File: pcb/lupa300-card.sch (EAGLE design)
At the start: 22 parts

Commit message: more work on lupa card
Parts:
- added C13, C14, C15, C16, C17, C18, C19, C20, C21, C22, C25, C26, C27, C28, C29, C30, C5, C6: (no value), rcl:C-EUC0603
- added C23, C24: (no value), rcl:C-EUC1206
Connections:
- new net N$2: C25.2, C27.2
- net 2.5V: now also U$1.VADC1, U$1.VDDA, U$1.VDDD, U$1.VDDO
- net GND: now also C13.2, C14.2, C15.2, C16.2, C17.2, C18.2, C19.2, C20.2, C21.2, C22.2, C23.2, C24.2, C26.2, C28.2, C29.2, C30.2, C5.2, C6.2
- net VADC: now also C20.1, C21.1, C22.1; no longer U$1.VADC1
- net VDDA: now also C14.1, C15.1, C16.1; no longer U$1.VDDA
- net VDDD: now also C13.1, C5.1, C6.1; no longer U$1.VDDD
- net VDDO: now also C17.1, C18.1, C19.1; no longer U$1.VDDO
- net VPIX: now also C25.1, C26.1, C27.1
- net VRAW: now also C23.1, C24.1
- net VRESET_1: now also C28.1, C29.1, C30.1

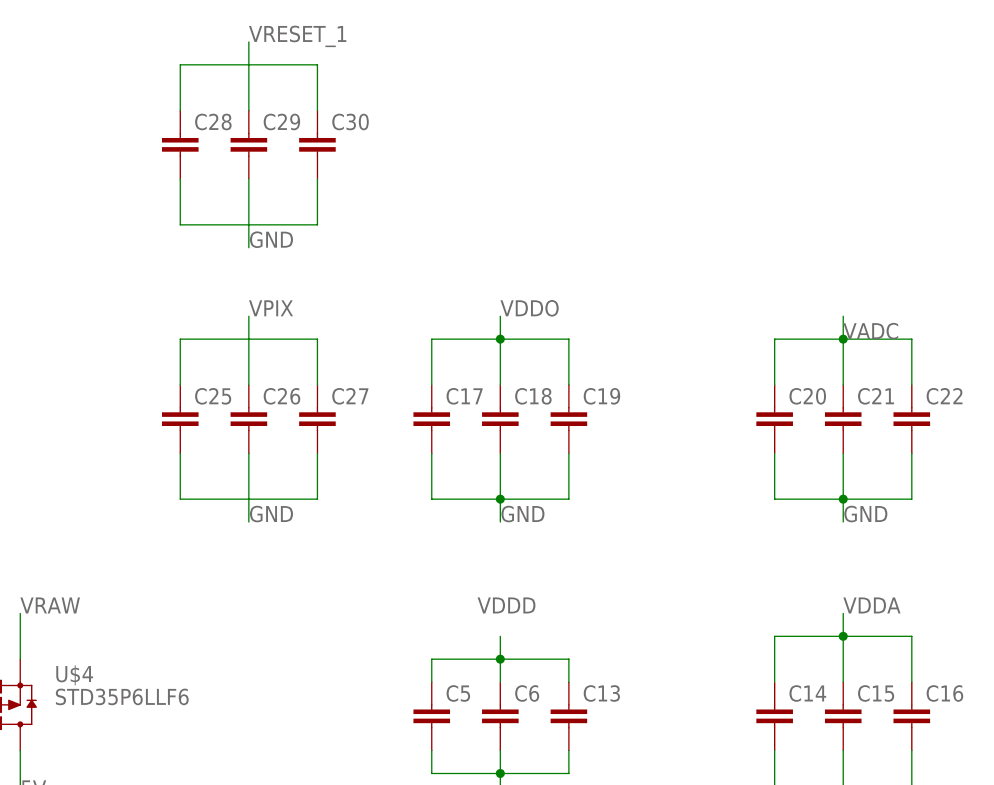
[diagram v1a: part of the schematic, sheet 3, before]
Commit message: made lupa card 4 layer
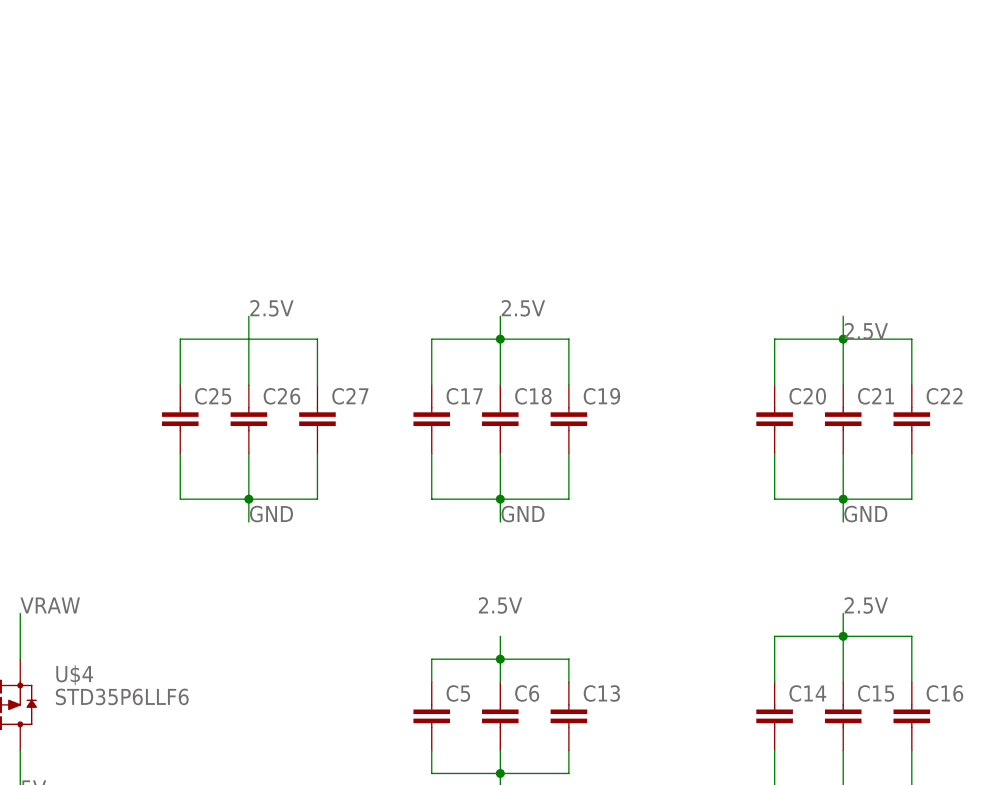
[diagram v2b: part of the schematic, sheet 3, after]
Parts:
- removed C28, C29, C30: (no value), rcl:C-EUC0603
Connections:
- removed net N$2: C25.2, C27.2
- removed net VADC: C20.1, C21.1, C22.1, R8.1, U$1.VADC, U$1.VADC2
- removed net VDDA: C14.1, C15.1, C16.1, R10.1, R11.1, R12.1, R9.1, U$1.VDDA1
- removed net VDDD: C13.1, C5.1, C6.1, U$1.VDDD1
- removed net VDDO: C17.1, C18.1, C19.1
- removed net VMEM_H: U$1.VMEM_H
- removed net VPIX: C25.1, C26.1, C27.1, R7.1, U$1.VPIX
- removed net VRESET_1: C28.1, C29.1, C30.1, U$1.VRESET_1
- net 2.5V: now also C13.1, C14.1, C15.1, C16.1, C17.1, C18.1, C19.1, C20.1, C21.1, C22.1, C25.1, C26.1, C27.1, C5.1, C6.1, R10.1, R11.1, R12.1, R7.1, R8.1, R9.1, U$1.VADC, U$1.VADC2, U$1.VDDA1, U$1.VDDD1, U$1.VPIX
- net 3V3: now also U$1.VMEM_H, U$1.VRESET_1
- net GND: now also C25.2, C27.2; no longer C28.2, C29.2, C30.2

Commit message: routed critical signals.
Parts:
- added C28, C29: (no value), rcl:C-EUC0603
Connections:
- net 3V3: now also C28.1, C29.1
- net GND: now also C28.2, C29.2
- net SPI_CLK: now also UZEDLOWER.14; no longer UZEDLOWER.3
- net SPI_DATA: now also UZEDLOWER.16; no longer UZEDLOWER.5
- net SPI_EN: now also UZEDLOWER.12; no longer UZEDLOWER.1
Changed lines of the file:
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@@
 <part name="C26" library="rcl" library_urn="urn:adsk.eagle:library:334" deviceset="C-EU" device="C0603" package3d_urn="urn:adsk.eagle:package:23616/2"/>
 <part name="C27" library="rcl" library_urn="urn:adsk.eagle:library:334" deviceset="C-EU" device="C0603" package3d_urn="urn:adsk.eagle:package:23616/2"/>
+<part name="C28" library="rcl" library_urn="urn:adsk.eagle:library:334" deviceset="C-EU" device="C0603" package3d_urn="urn:adsk.eagle:package:23616/2"/>
+<part name="C29" library="rcl" library_urn="urn:adsk.eagle:library:334" deviceset="C-EU" device="C0603" package3d_urn="urn:adsk.eagle:package:23616/2"/>
 </parts>
 <sheets>
@@
 <instance part="C26" gate="G$1" x="53.34" y="111.76"/>
 <instance part="C27" gate="G$1" x="60.96" y="111.76"/>
+<instance part="C28" gate="G$1" x="13.97" y="113.03"/>
+<instance part="C29" gate="G$1" x="22.86" y="113.03"/>
 </instances>
 <busses>
@@
 <junction x="53.34" y="101.6"/>
 </segment>
+<segment>
+<pinref part="C28" gate="G$1" pin="2"/>
+<wire x1="13.97" y1="107.95" x2="13.97" y2="104.14" width="0.1524" layer="91"/>
+<wire x1="13.97" y1="104.14" x2="17.78" y2="104.14" width="0.1524" layer="91"/>
+<pinref part="C29" gate="G$1" pin="2"/>
+<wire x1="17.78" y1="104.14" x2="22.86" y2="104.14" width="0.1524" layer="91"/>
+<wire x1="22.86" y1="104.14" x2="22.86" y2="107.95" width="0.1524" layer="91"/>
+<wire x1="17.78" y1="104.14" x2="17.78" y2="101.6" width="0.1524" layer="91"/>
+</segment>
 </net>
 <net name="3V3" class="0">
@@
 <wire x1="81.28" y1="40.64" x2="81.28" y2="45.72" width="0.1524" layer="91"/>
 <label x="81.28" y="45.72" size="1.778" layer="95"/>
+</segment>
+<segment>
+<pinref part="C29" gate="G$1" pin="1"/>
+<wire x1="22.86" y1="115.57" x2="22.86" y2="119.38" width="0.1524" layer="91"/>
+<wire x1="22.86" y1="119.38" x2="19.05" y2="119.38" width="0.1524" layer="91"/>
+<pinref part="C28" gate="G$1" pin="1"/>
+<wire x1="19.05" y1="119.38" x2="13.97" y2="119.38" width="0.1524" layer="91"/>
+<wire x1="13.97" y1="119.38" x2="13.97" y2="115.57" width="0.1524" layer="91"/>
+<wire x1="19.05" y1="119.38" x2="19.05" y2="121.92" width="0.1524" layer="91"/>
 </segment>
 </net>
@@
 </segment>
 </net>
-<net name="SPI_DATA" class="0">
-<segment>
-<pinref part="UZEDLOWER" gate="G$1" pin="5"/>
-<wire x1="55.88" y1="50.8" x2="50.8" y2="50.8" width="0.1524" layer="91"/>
-<label x="35.56" y="50.8" size="1.778" layer="95"/>
-</segment>
-</net>
-<net name="SPI_CLK" class="0">
-<segment>
-<pinref part="UZEDLOWER" gate="G$1" pin="3"/>
-<wire x1="55.88" y1="53.34" x2="50.8" y2="53.34" width="0.1524" layer="91"/>
-<label x="35.56" y="53.34" size="1.778" layer="95"/>
-</segment>
-</net>
-<net name="SPI_EN" class="0">
-<segment>
-<pinref part="UZEDLOWER" gate="G$1" pin="1"/>
-<wire x1="55.88" y1="55.88" x2="50.8" y2="55.88" width="0.1524" layer="91"/>
-<label x="35.56" y="55.88" size="1.778" layer="95"/>
-</segment>
-</net>
 <net name="VRAW" class="0">
 <segment>
@@
 </segment>
 </net>
+<net name="SPI_EN" class="0">
+<segment>
+<pinref part="UZEDLOWER" gate="G$1" pin="12"/>
+<wire x1="71.12" y1="43.18" x2="76.2" y2="43.18" width="0.1524" layer="91"/>
+<label x="78.74" y="43.18" size="1.778" layer="95"/>
+</segment>
+</net>
+<net name="SPI_CLK" class="0">
+<segment>
+<pinref part="UZEDLOWER" gate="G$1" pin="14"/>
+<wire x1="71.12" y1="40.64" x2="76.2" y2="40.64" width="0.1524" layer="91"/>
+<label x="78.74" y="40.64" size="1.778" layer="95"/>
+</segment>
+</net>
+<net name="SPI_DATA" class="0">
+<segment>
+<pinref part="UZEDLOWER" gate="G$1" pin="16"/>
+<wire x1="71.12" y1="38.1" x2="76.2" y2="38.1" width="0.1524" layer="91"/>
+<label x="78.74" y="38.1" size="1.778" layer="95"/>
+</segment>
+</net>

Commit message: finalized design
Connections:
- net FRAME_VALID: now also UZEDLOWER.12; no longer UZEDLOWER.10
- net INT_TIME1: now also UZEDLOWER.9; no longer UZEDLOWER.11
- net INT_TIME2: now also UZEDLOWER.10; no longer UZEDLOWER.13
- net INT_TIME3: now also UZEDLOWER.11; no longer UZEDLOWER.15
- net LINE_VALID: now also UZEDLOWER.13; no longer UZEDLOWER.9
- net SPI_CLK: now also UZEDLOWER.15; no longer UZEDLOWER.14
- net SPI_DATA: now also UZEDLOWER.14; no longer UZEDLOWER.16
- net SPI_EN: now also UZEDLOWER.16; no longer UZEDLOWER.12
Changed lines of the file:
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@@
 <?xml version="1.0" encoding="utf-8"?>
 <!DOCTYPE eagle SYSTEM "eagle.dtd">
-<eagle version="8.5.0">
+<eagle version="8.3.1">
 <drawing>
 <settings>
@@
 <wire x1="22.86" y1="104.14" x2="22.86" y2="107.95" width="0.1524" layer="91"/>
 <wire x1="17.78" y1="104.14" x2="17.78" y2="101.6" width="0.1524" layer="91"/>
+<label x="17.78" y="101.6" size="1.778" layer="95"/>
 </segment>
 </net>
@@
 <wire x1="13.97" y1="119.38" x2="13.97" y2="115.57" width="0.1524" layer="91"/>
 <wire x1="19.05" y1="119.38" x2="19.05" y2="121.92" width="0.1524" layer="91"/>
+<label x="19.05" y="121.92" size="1.778" layer="95"/>
 </segment>
 </net>
@@
 </segment>
 </net>
+<net name="VRAW" class="0">
+<segment>
+<pinref part="UZEDLOWER" gate="G$1" pin="7"/>
+<wire x1="55.88" y1="48.26" x2="50.8" y2="48.26" width="0.1524" layer="91"/>
+<label x="35.56" y="48.26" size="1.778" layer="95"/>
+</segment>
+<segment>
+<pinref part="UZEDLOWER" gate="G$1" pin="8"/>
+<wire x1="71.12" y1="48.26" x2="76.2" y2="48.26" width="0.1524" layer="91"/>
+<label x="78.74" y="48.26" size="1.778" layer="95"/>
+</segment>
+</net>
+<net name="MOSFET_CTRL" class="0">
+<segment>
+<pinref part="UZEDLOWER" gate="G$1" pin="6"/>
+<wire x1="86.36" y1="50.8" x2="71.12" y2="50.8" width="0.1524" layer="91"/>
+<label x="86.36" y="50.8" size="1.778" layer="95"/>
+</segment>
+</net>
 <net name="INT_TIME1" class="0">
+<segment>
+<pinref part="UZEDLOWER" gate="G$1" pin="9"/>
+<wire x1="55.88" y1="45.72" x2="50.8" y2="45.72" width="0.1524" layer="91"/>
+<label x="35.56" y="45.72" size="1.778" layer="95"/>
+</segment>
+</net>
+<net name="INT_TIME3" class="0">
 <segment>
 <pinref part="UZEDLOWER" gate="G$1" pin="11"/>
@@
 </segment>
 </net>
-<net name="INT_TIME2" class="0">
+<net name="LINE_VALID" class="0">
 <segment>
 <pinref part="UZEDLOWER" gate="G$1" pin="13"/>
@@
 </segment>
 </net>
-<net name="INT_TIME3" class="0">
+<net name="SPI_CLK" class="0">
 <segment>
 <pinref part="UZEDLOWER" gate="G$1" pin="15"/>
@@
 </segment>
 </net>
+<net name="SPI_EN" class="0">
+<segment>
+<pinref part="UZEDLOWER" gate="G$1" pin="16"/>
+<wire x1="71.12" y1="38.1" x2="76.2" y2="38.1" width="0.1524" layer="91"/>
+<label x="78.74" y="38.1" size="1.778" layer="95"/>
+</segment>
+</net>
+<net name="SPI_DATA" class="0">
+<segment>
+<pinref part="UZEDLOWER" gate="G$1" pin="14"/>
+<wire x1="71.12" y1="40.64" x2="76.2" y2="40.64" width="0.1524" layer="91"/>
+<label x="78.74" y="40.64" size="1.778" layer="95"/>
+</segment>
+</net>
 <net name="FRAME_VALID" class="0">
+<segment>
+<pinref part="UZEDLOWER" gate="G$1" pin="12"/>
+<wire x1="71.12" y1="43.18" x2="76.2" y2="43.18" width="0.1524" layer="91"/>
+<label x="78.74" y="43.18" size="1.778" layer="95"/>
+</segment>
+</net>
+<net name="INT_TIME2" class="0">
 <segment>
 <pinref part="UZEDLOWER" gate="G$1" pin="10"/>
 <wire x1="71.12" y1="45.72" x2="76.2" y2="45.72" width="0.1524" layer="91"/>
 <label x="78.74" y="45.72" size="1.778" layer="95"/>
-</segment>
-</net>
-<net name="LINE_VALID" class="0">
-<segment>
-<pinref part="UZEDLOWER" gate="G$1" pin="9"/>
-<wire x1="55.88" y1="45.72" x2="50.8" y2="45.72" width="0.1524" layer="91"/>
-<label x="35.56" y="45.72" size="1.778" layer="95"/>
-</segment>
-</net>
-<net name="VRAW" class="0">
-<segment>
-<pinref part="UZEDLOWER" gate="G$1" pin="7"/>
-<wire x1="55.88" y1="48.26" x2="50.8" y2="48.26" width="0.1524" layer="91"/>
-<label x="35.56" y="48.26" size="1.778" layer="95"/>
-</segment>
-<segment>
-<pinref part="UZEDLOWER" gate="G$1" pin="8"/>
-<wire x1="71.12" y1="48.26" x2="76.2" y2="48.26" width="0.1524" layer="91"/>
-<label x="78.74" y="48.26" size="1.778" layer="95"/>
-</segment>
-</net>
-<net name="MOSFET_CTRL" class="0">
-<segment>
-<pinref part="UZEDLOWER" gate="G$1" pin="6"/>
-<wire x1="86.36" y1="50.8" x2="71.12" y2="50.8" width="0.1524" layer="91"/>
-<label x="86.36" y="50.8" size="1.778" layer="95"/>
-</segment>
-</net>
-<net name="SPI_EN" class="0">
-<segment>
-<pinref part="UZEDLOWER" gate="G$1" pin="12"/>
-<wire x1="71.12" y1="43.18" x2="76.2" y2="43.18" width="0.1524" layer="91"/>
-<label x="78.74" y="43.18" size="1.778" layer="95"/>
-</segment>
-</net>
-<net name="SPI_CLK" class="0">
-<segment>
-<pinref part="UZEDLOWER" gate="G$1" pin="14"/>
-<wire x1="71.12" y1="40.64" x2="76.2" y2="40.64" width="0.1524" layer="91"/>
-<label x="78.74" y="40.64" size="1.778" layer="95"/>
-</segment>
-</net>
-<net name="SPI_DATA" class="0">
-<segment>
-<pinref part="UZEDLOWER" gate="G$1" pin="16"/>
-<wire x1="71.12" y1="38.1" x2="76.2" y2="38.1" width="0.1524" layer="91"/>
-<label x="78.74" y="38.1" size="1.778" layer="95"/>
 </segment>
 </net>
@@
 packages will not be understood (or retained) with this version.
 </note>
-<note version="8.4" severity="warning">
-Since Version 8.4, EAGLE supports properties for SPICE simulation.
-Probes in schematics and SPICE mapping objects found in parts and library devices
-will not be understood with this version. Update EAGLE to the latest version
-for full support of SPICE simulation.
-</note>
 </compatibility>
